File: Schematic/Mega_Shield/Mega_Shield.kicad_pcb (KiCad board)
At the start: 2 copper layers, 132.5 x 74.9 mm, 24 parts, among them J1 Mini-DIN-4, J10 Conn_01x08, J11 Conn_01x08, J12 Conn_02x18_Odd_Even, J13 Conn_01x08, J14 Conn_01x08, J15 Conn_01x08, J16 Conn_01x10, J2 Mini-DIN-4, J3 Mini-DIN-4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

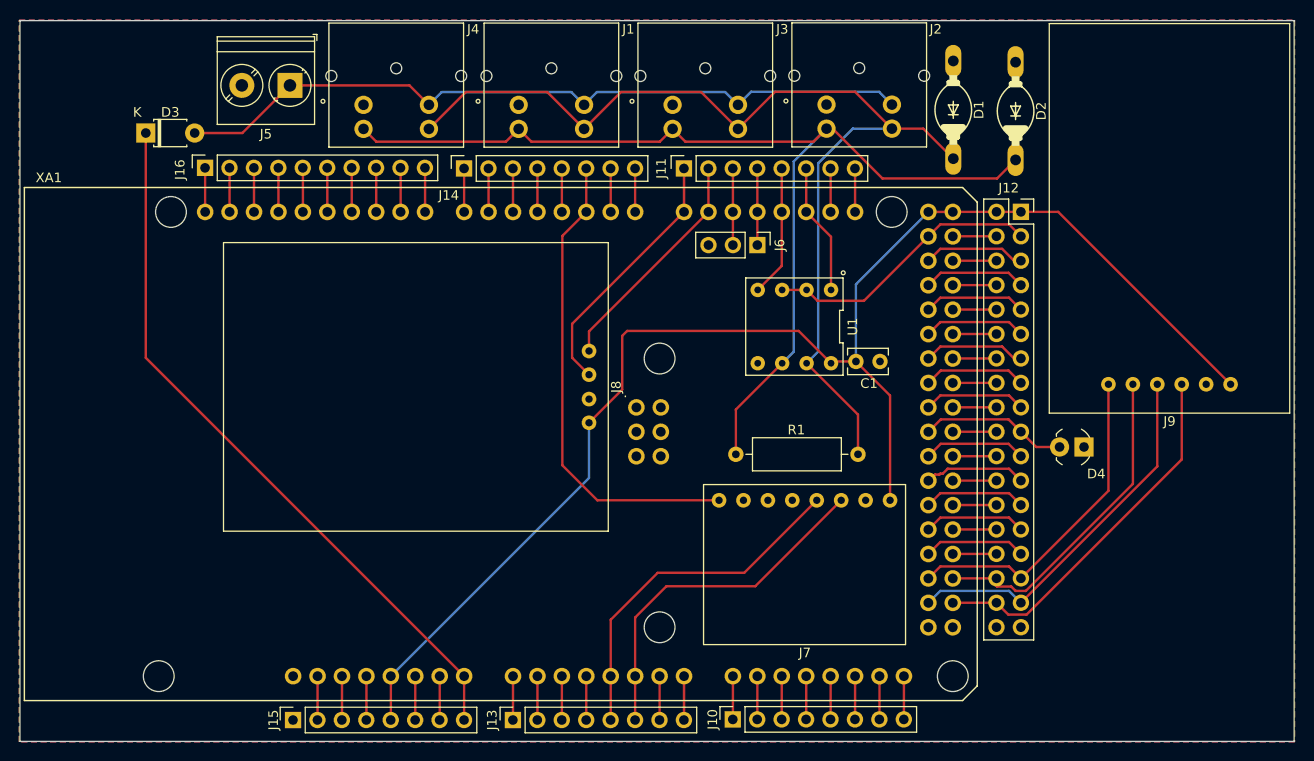
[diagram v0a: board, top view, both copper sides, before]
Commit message: Updating schematic with Oshpark/Digikey order
Updates to add various components and capability.

2.2 Basic Sensor Suite
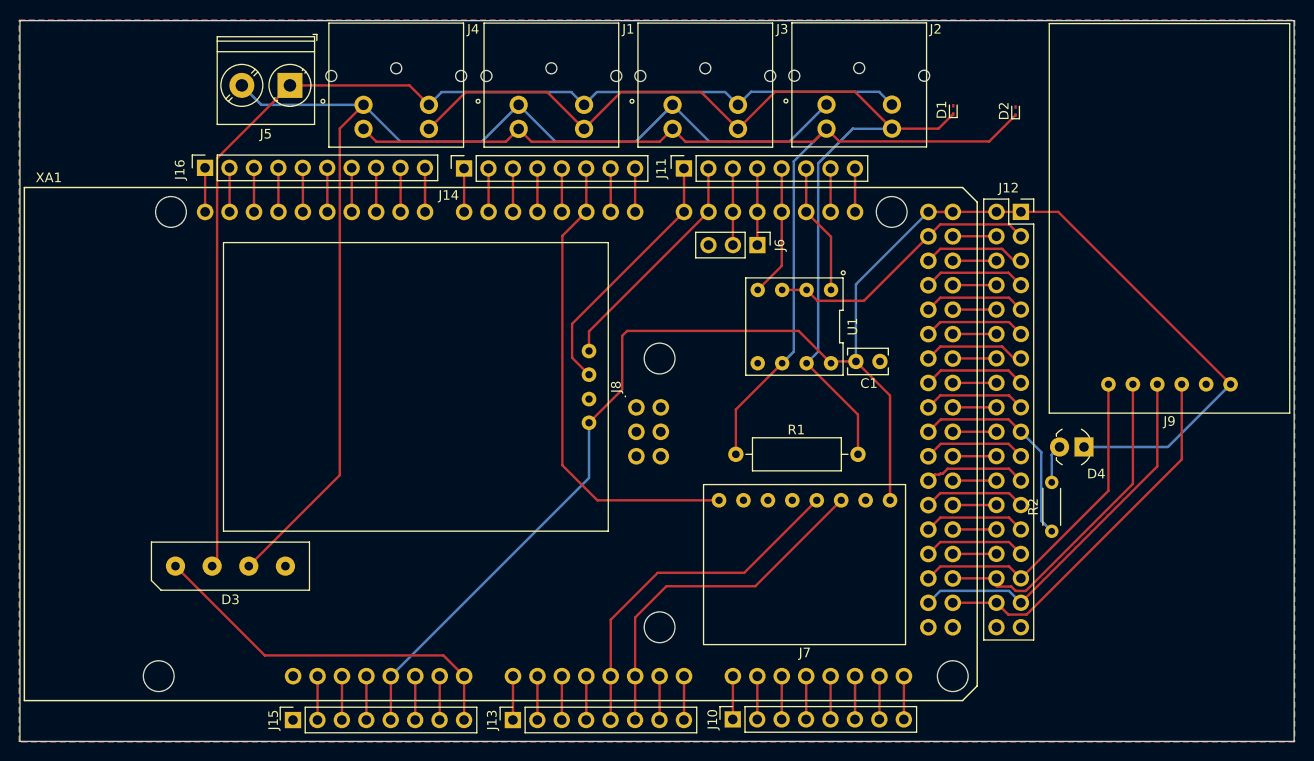
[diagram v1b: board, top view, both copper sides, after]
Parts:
- added R2: 4.7k, Resistor_THT:R_Axial_DIN0204_L3.6mm_D1.6mm_P5.08mm_Horizontal, F.Cu at (188.2, 70.9)
- D1, D2: footprint TTS-UART:DO204-10 -> Diode_SMD:D_SOD-923
- D3: value D -> D_Bridge_+AA-; footprint Diode_THT:D_T-1_P5.08mm_Horizontal -> TTS-UART:KBP306GTB
- moved D3 45.9 mm to (102.8, 74.5)
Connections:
- D4 pad 1: GND -> VCC
- D4 pad 2: /D38 -> Net-(D4-Pad2)
- J1 pad 1: GND -> Net-(D3-Pad3)
- J15 pad 1: Net-(J15-Pad1) -> (no net)
- J2 pad 1: GND -> Net-(D3-Pad3)
- J3 pad 1: GND -> Net-(D3-Pad3)
- J4 pad 1: GND -> Net-(D3-Pad3)
- J5 pad 2: GND -> Net-(D3-Pad3)
- J7 pad 3: Net-(J7-Pad3) -> (no net)
- J7 pad 4: Net-(J7-Pad4) -> (no net)
- XA1 pad 5V2: Net-(XA1-Pad5V2) -> (no net)
- XA1 pad GND4: Net-(XA1-PadGND4) -> (no net)
- XA1 pad MISO: Net-(XA1-PadMISO) -> (no net)
- XA1 pad MOSI: Net-(XA1-PadMOSI) -> (no net)
- XA1 pad RST2: Net-(XA1-PadRST2) -> (no net)
- XA1 pad SCK: Net-(XA1-PadSCK) -> (no net)
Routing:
- net Net-(D3-Pad3): track 0.00 -> 124.0 mm
- net Net-(D3-Pad2): track 78.7 -> 120.1 mm
- net /VIN: track 74.7 -> 39.3 mm
- net VCC: track 149.3 -> 167.2 mm
- net /D38: track 15.4 -> 22.4 mm
- net Net-(D4-Pad2): track 0.00 -> 4.02 mm
- net Net-(D2-Pad1): track 111.8 -> 110.6 mm
- net Net-(D1-Pad1): track 107.5 -> 106.8 mm

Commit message: Fixed schematic issues. Made code for TTS transmit
Schematic issues documented on Trello card fixed. TTS differential wire transmit code for the TTS implemented. Still need to do auto adressing and time stamp transmission.

2.2 Basic Sensor Suite
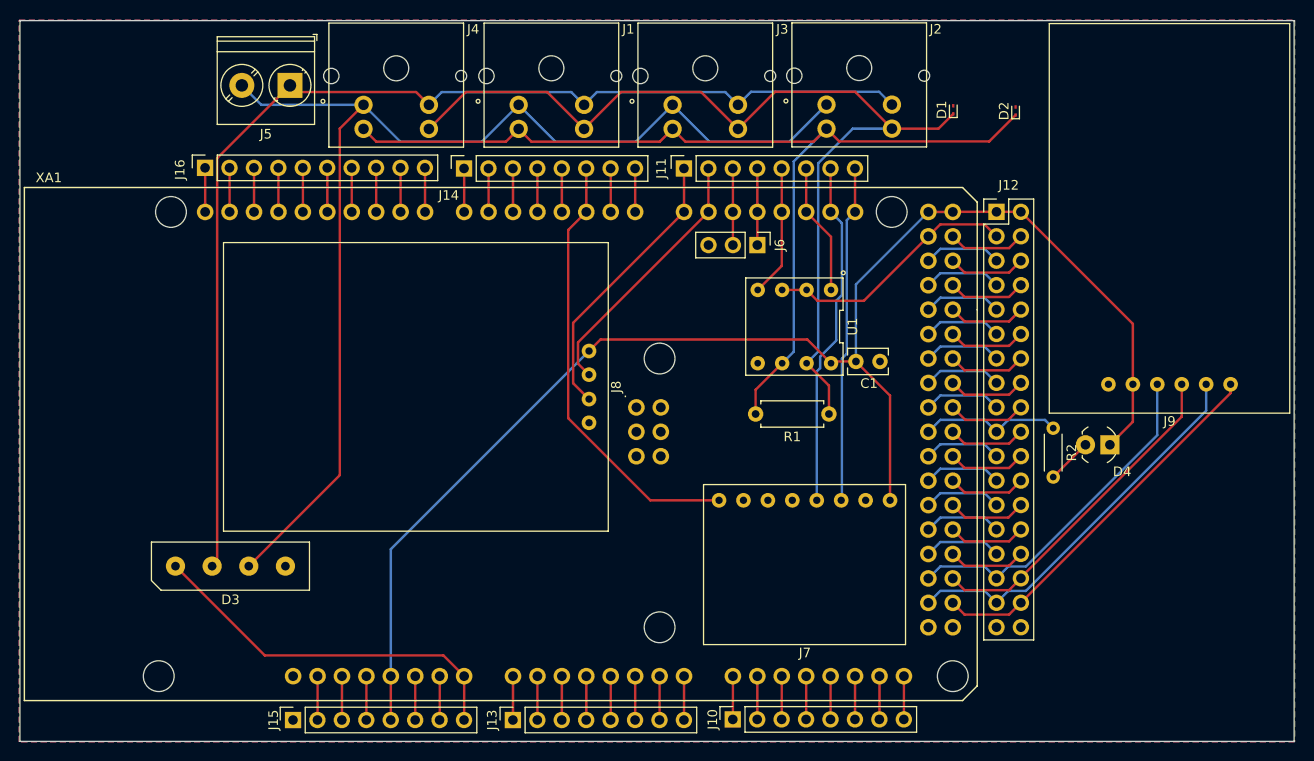
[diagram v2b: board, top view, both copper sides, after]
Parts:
- J12: footprint Connector_PinSocket_2.54mm:PinSocket_2x18_P2.54mm_Vertical -> TTS-UART:PinSocket_2x18_P2.54mm_Vertical_Swapped
- R1: footprint Resistor_THT:R_Axial_DIN0309_L9.0mm_D3.2mm_P12.70mm_Horizontal -> Resistor_THT:R_Axial_DIN0207_L6.3mm_D2.5mm_P7.62mm_Horizontal
- moved R2 10.7 mm to (188.3, 60.1), turned to 270 degrees
- moved R1 5.17 mm to (165.0, 58.7)
- moved D4 2.70 mm to (191.7, 61.9)
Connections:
- J7 pad 5: /A4 -> /D20
- J7 pad 6: /A5 -> /D21
- J8 pad 1: /D15 -> VCC
- J8 pad 2: /D14 -> /D15
- J8 pad 3: GND -> /D14
- J8 pad 4: VCC -> GND
- J9 pad 1: VCC -> /D53
- J9 pad 2: GND -> /D52
- J9 pad 3: /D53 -> /D51
- J9 pad 4: /D52 -> /D50
- J9 pad 5: /D51 -> VCC
- J9 pad 6: /D50 -> GND
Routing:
- net /A5: track 37.1 -> 4.57 mm
- net /A4: track 37.0 -> 4.57 mm
- net /D20: track 4.52 -> 36.1 mm
- net /D21: track 4.52 -> 35.1 mm
- net VCC: track 167.2 -> 150.5 mm
- net /D38: track 22.4 -> 14.9 mm
- net Net-(D1-Pad1): track 106.8 -> 101.4 mm
- net Net-(D2-Pad1): track 110.6 -> 105.5 mm
- net /D2: track 49.7 -> 46.0 mm
- net /D45: track 4.55 -> 8.16 mm
- net /D37: track 4.55 -> 8.16 mm
- net /D27: track 4.55 -> 8.11 mm
- net /D47: track 4.55 -> 8.10 mm
- net /D43: track 4.55 -> 8.10 mm
- net /D41: track 4.55 -> 8.10 mm
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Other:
- board text added: "0.2.1.b"

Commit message: Upadeted PCB design for Logger and for TTS
Mega updated for BLE and reduced in size. Nano shield updated for
MLX90621 array based sensor
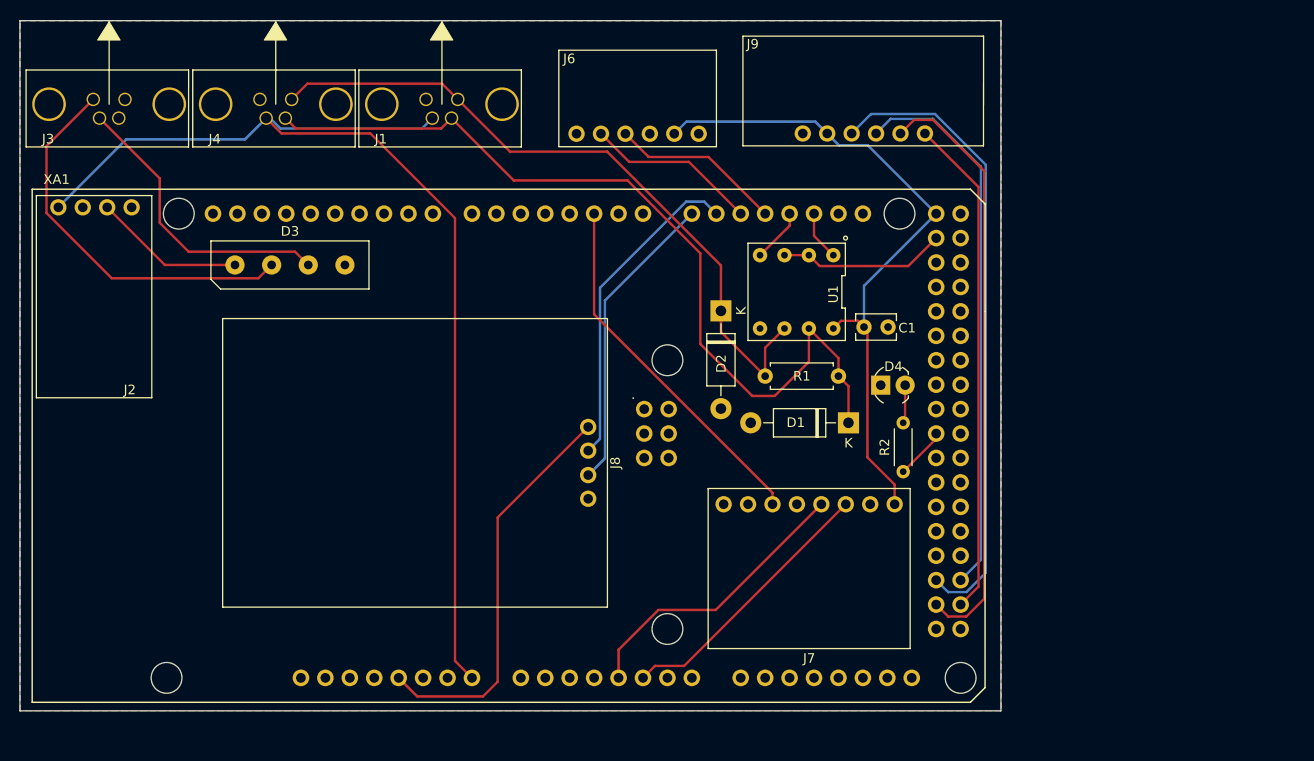
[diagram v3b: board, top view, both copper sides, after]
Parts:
- removed J10, J11, J13, J14, J15: Conn_01x08, Connector_PinSocket_2.54mm:PinSocket_1x08_P2.54mm_Vertical
- removed J12: Conn_02x18_Odd_Even, TTS-UART:PinSocket_2x18_P2.54mm_Vertical_Swapped
- removed J16: Conn_01x10, Connector_PinSocket_2.54mm:PinSocket_1x10_P2.54mm_Vertical
- removed J5: Screw_Terminal_01x02, TerminalBlock_Phoenix:TerminalBlock_Phoenix_PT-1,5-2-5.0-H_1x02_P5.00mm_Horizontal
- D1, D2: footprint Diode_SMD:D_SOD-923 -> Diode_THT:D_DO-41_SOD81_P10.16mm_Horizontal
- D3: footprint TTS-UART:KBP306GTB -> TTS-URAT:KBP306GTB
- D4: footprint digikey-kicad-library:LED_3mm_Radial -> Digikey:LED_3mm_Radial
- J1, J3, J4: footprint TTS-UART:KMDGX-4S-BS -> TTS-URAT:RHT-634-1261-1
- J2: value Mini-DIN-4 -> Conn_01x04_Female; footprint TTS-UART:KMDGX-4S-BS -> Onboard_Sensors:Voltage_Regulator
- J6: value SF_OBDII -> BLE HC-05; footprint Connector_PinHeader_2.54mm:PinHeader_1x03_P2.54mm_Vertical -> Onboard_Sensors:BLEHC-05
- J7: value GY-521 -> MPU 6050
- J9: footprint Onboard_Sensors:SD_Module -> Onboard_Sensors:SD_Module_Vertical
- U1: footprint TTS-UART:ISL81487EIPZ-PDIP -> TTS-URAT:ISL81487EIPZ-PDIP
- moved J2 87.4 mm to (82.6, 36.0), turned to 90 degrees
- moved J3 62.5 mm to (90.2, 26.5), turned to 180 degrees
- moved D2 37.0 mm to (153.8, 48.0), turned to 270 degrees
- moved D1 34.3 mm to (167.0, 59.6), turned to 180 degrees
- moved J9 32.5 mm to (168.5, 30.9)
- moved D3 31.9 mm to (109.0, 43.2)
- moved D4 19.7 mm to (172.9, 55.7), turned to 0 degrees
- moved R2 16.2 mm to (172.7, 64.7), turned to 90 degrees
- moved J4 15.1 mm to (107.5, 26.5), turned to 180 degrees
- moved J1 14.2 mm to (124.8, 26.5), turned to 180 degrees
- moved J6 14.1 mm to (147.8, 30.9)
- moved J8 7.90 mm to (122.0, 63.8)
- moved R1 4.06 mm to (166.0, 54.7)
- moved C1 3.68 mm to (171.1, 49.6)
- moved U1 3.62 mm to (161.6, 46.0)
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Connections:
- D3 pad 1: /VIN -> Net-(D3-Pad1)
- D4 pad 1: VCC -> GND
- J1 pad 1: Net-(D3-Pad3) -> GND
- J1 pad 2: Net-(D3-Pad2) -> /VIN
- J2 pad 1: Net-(D3-Pad3) -> Net-(J2-Pad1)
- J2 pad 2: Net-(D3-Pad2) -> Net-(D3-Pad1)
- J2 pad 3: Net-(D2-Pad1) -> GND
- J2 pad 4: Net-(D1-Pad1) -> /VIN
- J3 pad 1: Net-(D3-Pad3) -> Net-(D3-Pad2)
- J3 pad 2: Net-(D3-Pad2) -> Net-(D3-Pad3)
- J3 pad 3: Net-(D2-Pad1) -> Net-(J3-Pad3)
- J3 pad 4: Net-(D1-Pad1) -> Net-(J3-Pad4)
- J4 pad 1: Net-(D3-Pad3) -> GND
- J4 pad 2: Net-(D3-Pad2) -> /VIN
- J6 pad 1: /D17 -> Net-(J6-Pad1)
- J6 pad 3: GND -> /D17
- J7 pad 1: /D2 -> Net-(J7-Pad1)
- J7 pad 2: GND -> Net-(J7-Pad2)
- J7 pad 3: (no net) -> /D2
- J7 pad 4: (no net) -> GND
- J7 pad 5: /D20 -> /A4
- J7 pad 6: /D21 -> /A5
- XA1 pad 3V3: /3V3 -> VDD
- XA1 pad 5V2: (no net) -> Net-(XA1-Pad5V2)
- XA1 pad GND4: (no net) -> Net-(XA1-PadGND4)
- XA1 pad MISO: (no net) -> Net-(XA1-PadMISO)
- XA1 pad MOSI: (no net) -> Net-(XA1-PadMOSI)
- XA1 pad RST2: (no net) -> Net-(XA1-PadRST2)
- XA1 pad SCK: (no net) -> Net-(XA1-PadSCK)
- XA1 pad SCL: /SCL -> SCL
- XA1 pad SDA: /SDA -> SDA
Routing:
- net Net-(D3-Pad3): track 124.0 -> 30.7 mm
- net Net-(D3-Pad2): track 120.1 -> 40.6 mm
- net /VIN: track 39.3 -> 116.1 mm
- net VCC: track 150.5 -> 112.2 mm
- net /D20: track 36.1 -> 0.00 mm
- net /D21: track 35.1 -> 0.00 mm
- net Net-(D2-Pad1): track 105.5 -> 72.3 mm
- net /D50: track 36.3 -> 65.9 mm
- net /A4: track 4.57 -> 30.3 mm
- net /A5: track 4.57 -> 28.6 mm
- net /D51: track 35.2 -> 57.4 mm
- net /D52: track 40.9 -> 62.2 mm
- net Net-(D3-Pad1): track 0.00 -> 15.8 mm
- net GND: track 13.7 -> 0.00 mm
- net /D53: track 39.8 -> 52.0 mm
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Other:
- board size 132.5 x 74.9 mm -> 102 x 71.8 mm
- board text added: "0.2.1.C"
- board text removed: "0.2.1.b"

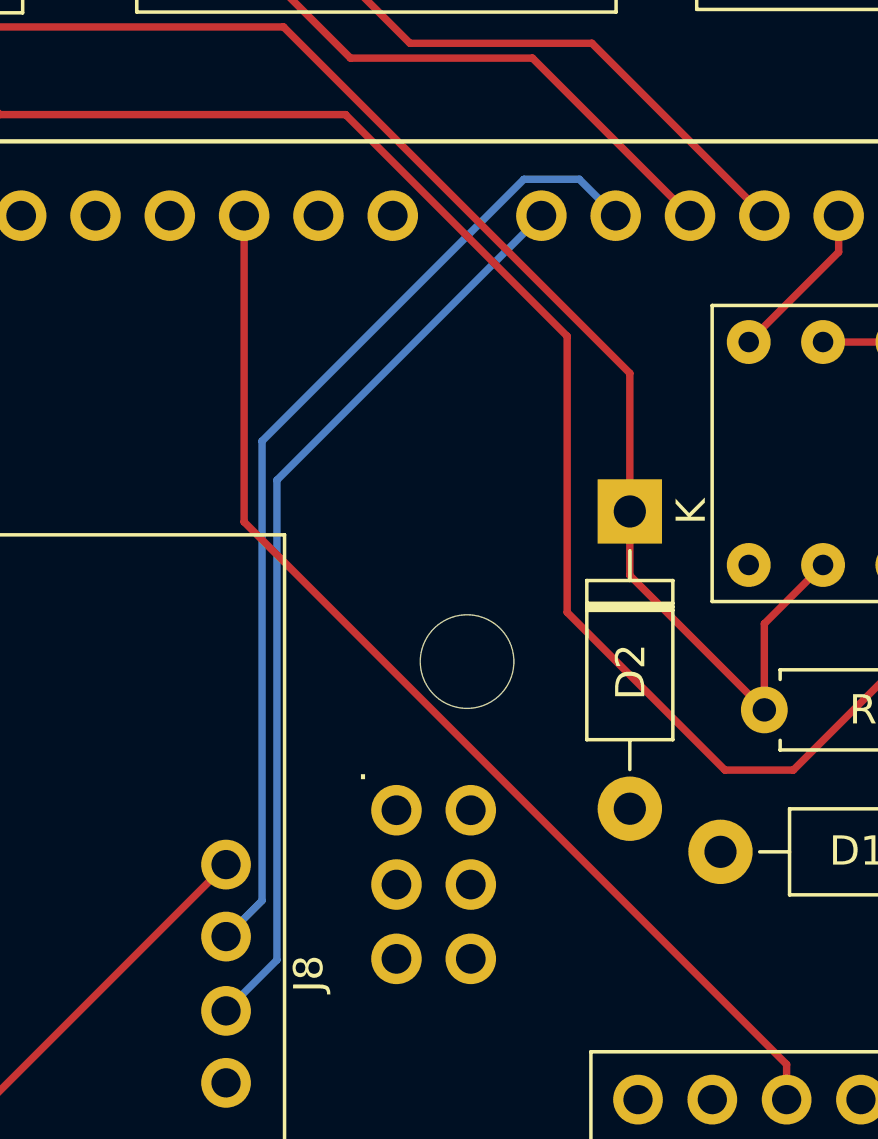
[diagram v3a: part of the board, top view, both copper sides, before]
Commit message: Udated logger and TTS for full sensor suit
2.2 Basic Sensor Suit and 2.6 Array Based Tire Temps
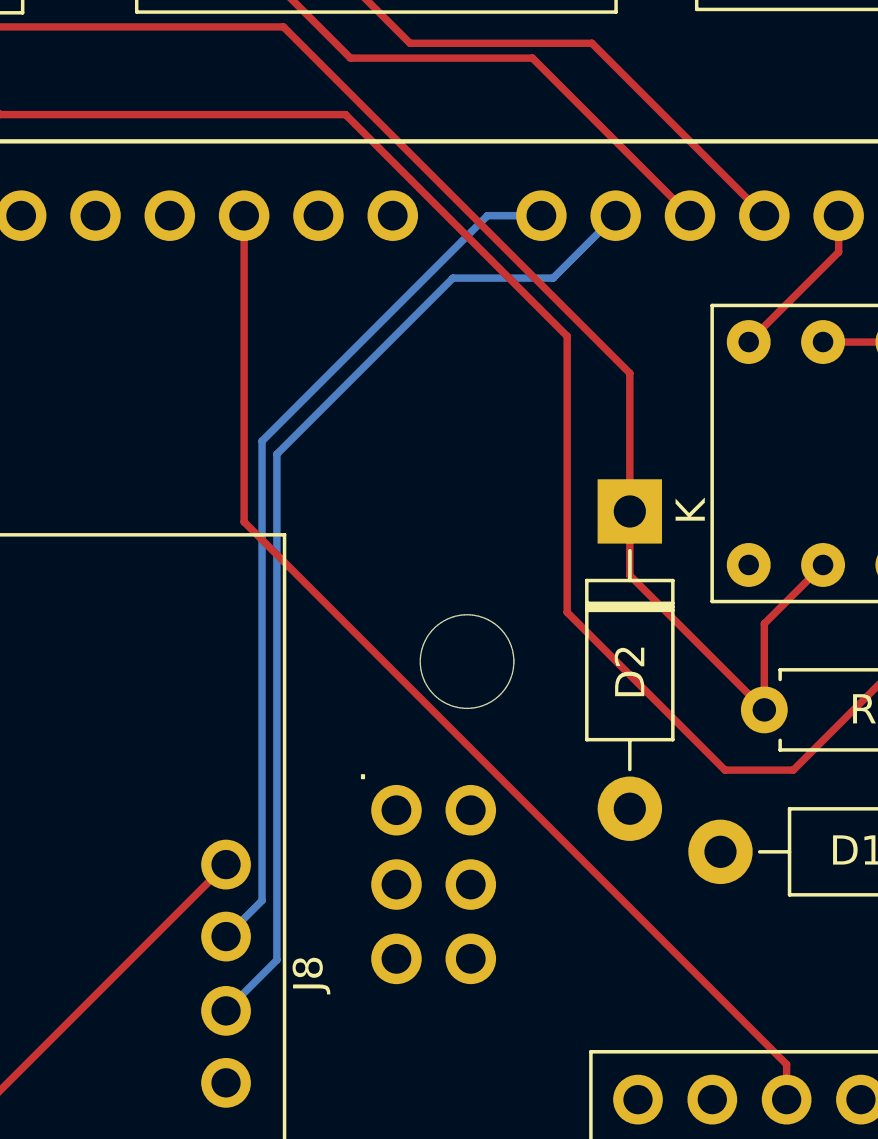
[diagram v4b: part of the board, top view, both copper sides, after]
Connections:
- J8 pad 2: /D15 -> /D14
- J8 pad 3: /D14 -> /D15
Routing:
- net /D14: track 31.6 -> 30.2 mm
- net /D15: track 33.8 -> 34.7 mm
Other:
- board text added: "0.2.1.D"
- board text removed: "0.2.1.C"
